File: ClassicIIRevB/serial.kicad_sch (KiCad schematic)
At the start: 35 parts, among them J2 MODEM, J3 PRINTER, U15 LM79L05AC, U3 AM26LV32, U5 AM26LV32, U6 AM26LS30, U7 AM26LS30, U8 Am85C80

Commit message: improved footprints and silkscreens
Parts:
- U8: footprint Package_LCC:PLCC-68_24.2x24.2mm_P1.27mm -> MyPackage:PLCC-68_24.2x24.2mm_P1.27mm_oval
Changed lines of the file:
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@@
 	(title_block
 		(title "Macintosh Classic II Revision B")
-		(date "2025-05-31")
+		(date "2025-06-04")
 		(company "Apple Computer")
 		(comment 1 "drawn by Bradley Bell")
@@
 			)
 		)
-		(property "Footprint" "Package_LCC:PLCC-68_24.2x24.2mm_P1.27mm"
+		(property "Footprint" "MyPackage:PLCC-68_24.2x24.2mm_P1.27mm_oval"
 			(at 128.27 184.15 0)
 			(effects

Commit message: Switch to some "official" net names
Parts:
- added TP10, TP64, TP65, TP9: ~, MyPackage:TestPoint_THTPad_D1.0mm_Drill0.5mm, symbol Connector:TestPoint
- added TP13, TP15, TP17: ~, MyPackage:TestPoint_Pad_D1.0mm, symbol Connector:TestPoint
- L1, L8, L9: value L_Ferrite_Small -> Ferrite
- renumbered TP51 to TP1, TP57 to TP11, TP97 to TP12, TP52 to TP18, TP56 to TP19, TP49 to TP2, TP53 to TP24, TP50 to TP3, TP48 to TP5, TP55 to TP6, TP54 to TP8, TP100 to TP83, TP142 to TP94
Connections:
- net ~{RTxCB} is gone; now on net C3_7M: U8.29 (~{RTxCB})
- net C3_7M: no longer U8.22 (PCLK)
- net GPIA: now also TP17.1
- net RxDB+: now also TP10.1
- net RxDB-: now also TP9.1
- net ~{DTRA}: now reaches TP94.1, U6.3 (InA), U8.19 (~{DTR/REQA})
- net RxDB: now reaches TP12.1, U3.13 (4Y), U8.28 (RxDB)
- net TxDA: now reaches TP83.1, U7.3 (InA), U8.18 (TxDA)
- net ~{RTSB}: now reaches TP99.1, U7.8 (In/~{EnC}), U8.24 (~{RTSB})
- net GPIAp renamed GPI
- net HSKIA renamed DTRA-
- net DTRA-: now also TP64.1
- net HSKIB renamed DTRB-
- net DTRB-: now also TP65.1
- net HSKOA renamed RxCA
- net RxCA: now also TP13.1
- net HSKOB renamed RxCB
- net RxCB: now also TP15.1
- net Ser_VCC renamed DRVR_VCC
- net Ser_VDD renamed RCVR_PWR
- net Ser_VEE renamed DRVR_VSS
- net ~{RTxCA} renamed SCCCLOCK
- new net C8M: U8.22 (PCLK)
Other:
- moved on the sheet: J3, RC1, TP11, TP12, TP18, TP19, TP24, TP6, TP8, TP83, TP94, TP99

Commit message: update exports
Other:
- title: Macintosh Classic II Revision B -> Macintosh Classic II (Later Revision)
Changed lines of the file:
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@@
 	(paper "USLetter")
 	(title_block
-		(title "Macintosh Classic II Revision B")
-		(date "2025-06-04")
+		(title "Macintosh Classic II (Later Revision)")
+		(date "2025-06-16")
 		(company "Apple Computer")
 		(comment 1 "drawn by Bradley Bell")

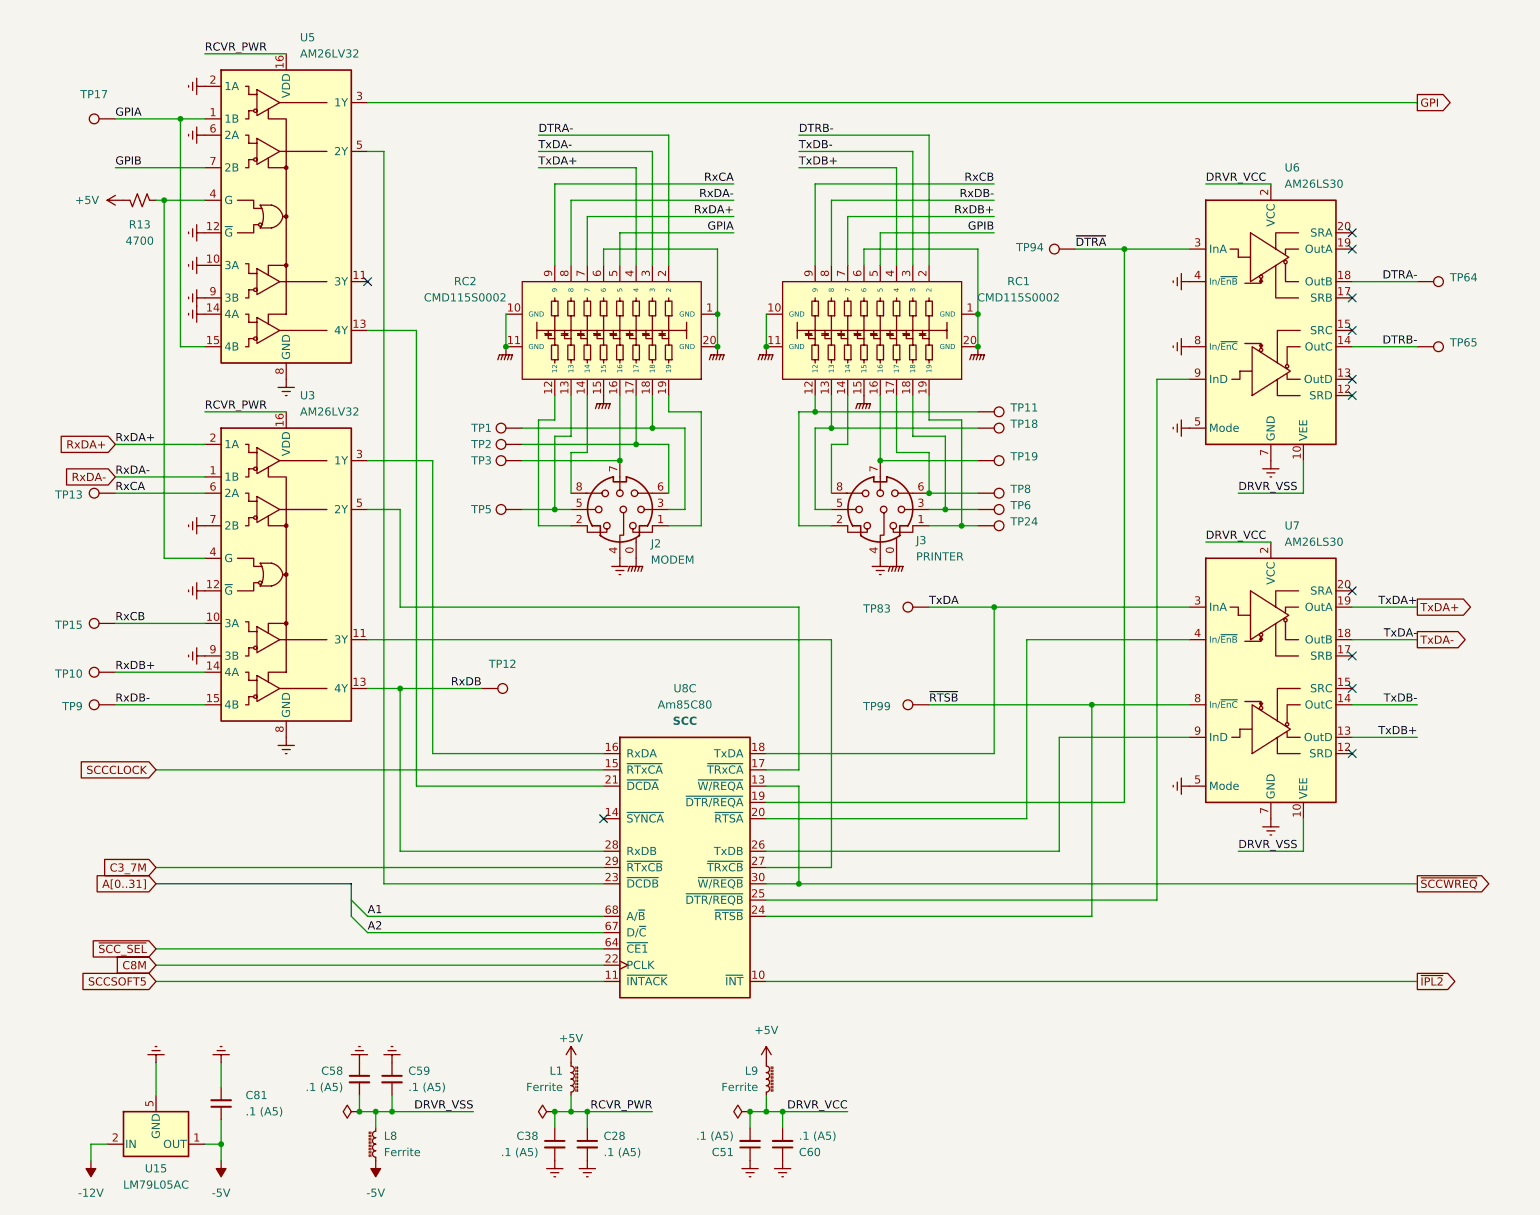
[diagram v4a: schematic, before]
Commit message: Corrections to SMDs, more improved footprints
The later revision board reproduction design is now complete.
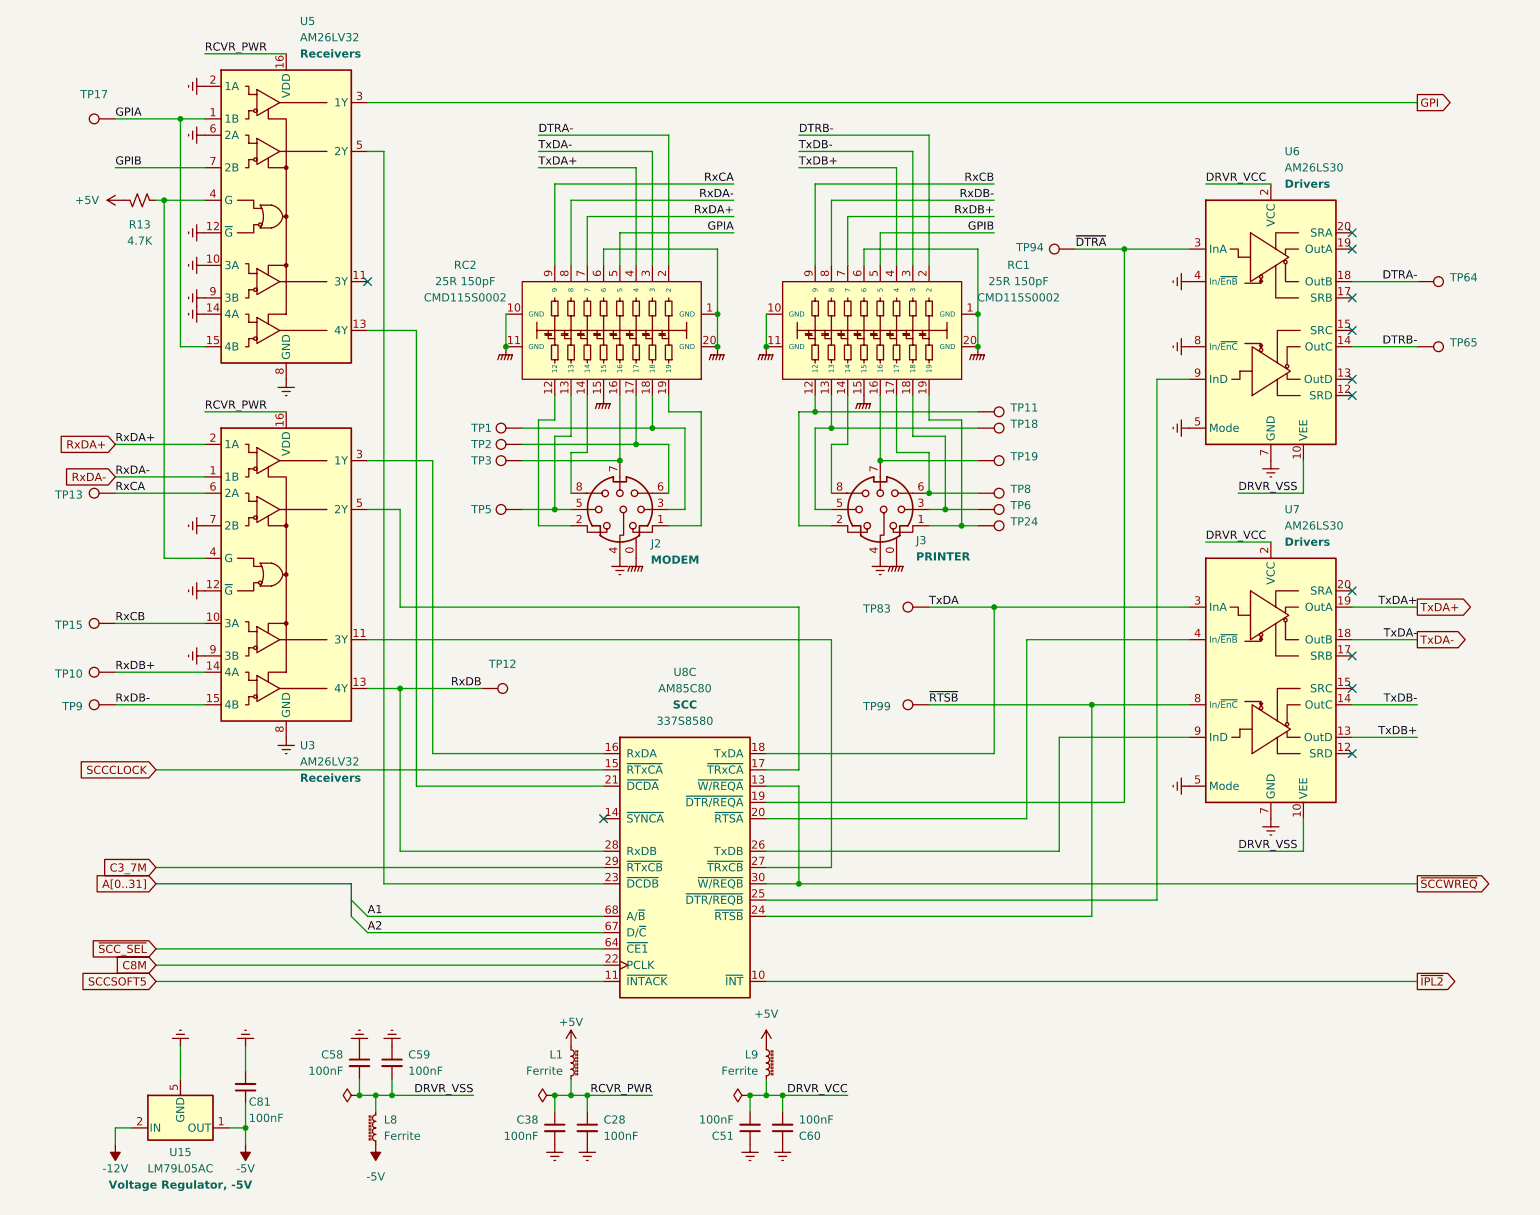
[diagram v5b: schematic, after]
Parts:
- C28, C38, C51, C58, C59, C60, C81: value .1 (A5) -> 100nF
- R13: value 4700 -> 4.7K
- RC1, RC2: value CMD115S0002 -> 25R 150pF; PartNum (none) -> CMD115S0002
- TP1, TP10, TP11, TP12, TP13, TP15, TP17, TP18, TP19, TP2, TP24, TP3, TP5, TP6, TP64, TP65, TP8, TP83, TP9, TP94, TP99: now left out of the parts list
- U8: value Am85C80 -> AM85C80; PartNum (none) -> 337S8580
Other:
- moved on the sheet: C28, C38, C51, C58, C59, C60, C81, L1, L8, L9, U15
